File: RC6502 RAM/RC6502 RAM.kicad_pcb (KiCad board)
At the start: 2 copper layers, 99.1 x 48.3 mm, 9 parts, among them J1 Page PullUp, J2 Bus enable, J3 CONN_01X39, U1 HM62256BLP-7, U2 74HCT00

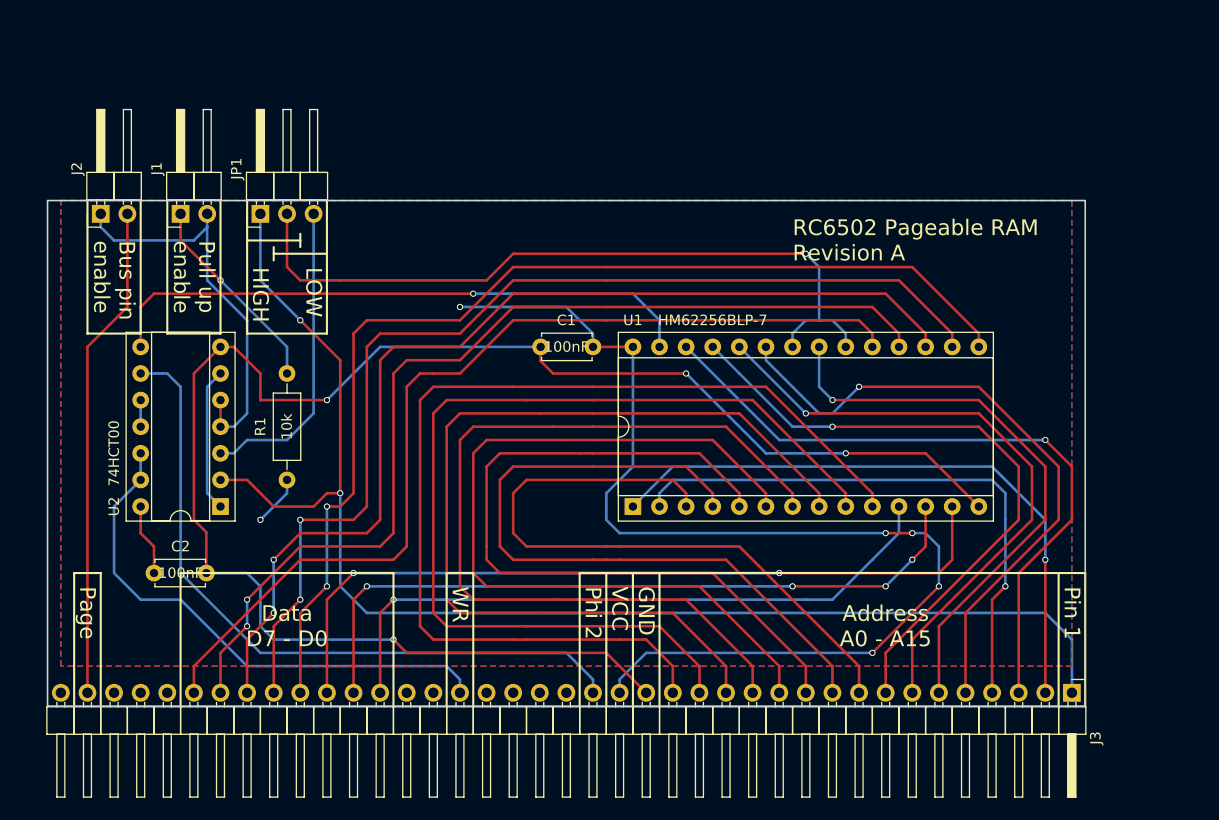
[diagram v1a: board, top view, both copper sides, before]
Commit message: RAM revision B
Fixed silkscreen notes by swapping high/low text, moved around tracks to make it a little more compact.
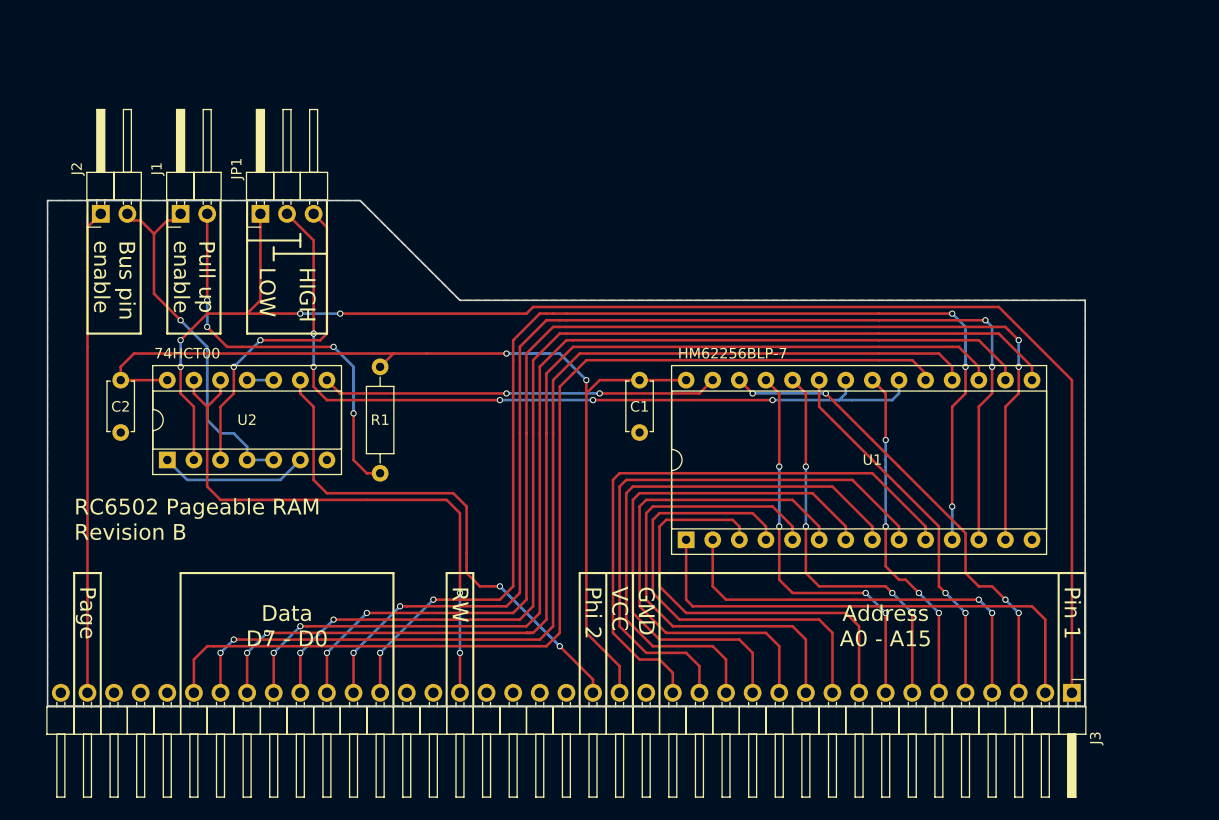
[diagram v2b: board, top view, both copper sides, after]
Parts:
- moved C2 18.7 mm to (95.9, 118.7), turned to 270 degrees
- moved R1 14.0 mm to (120.7, 117.5), turned to 270 degrees
- moved U2 6.75 mm to (100.3, 126.4), turned to 90 degrees
- moved U1 5.99 mm to (149.9, 134.0)
- moved C1 5.46 mm to (145.4, 118.7), turned to 270 degrees
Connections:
- net WR renamed RW
- J1 pad 1: Net-(J1-Pad1) -> PAGE
- J1 pad 2: PAGE -> Net-(J1-Pad2)
- J2 pad 1: PAGE -> Net-(J2-Pad1)
- J2 pad 2: Net-(J2-Pad2) -> PAGE
- J3 pad 38: Net-(J2-Pad2) -> Net-(J2-Pad1)
- R1 pad 2: Net-(J1-Pad1) -> Net-(J1-Pad2)
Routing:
- net GND: track 157.3 -> 0.00 mm, vias 4 -> 0
- net Net-(J2-Pad2): track 47.3 -> 0.00 mm
- net Net-(J2-Pad1): track 0.00 -> 46.2 mm
- net D0: track 62.8 -> 108.2 mm, vias 1 -> 5
- net D1: track 69.4 -> 112.8 mm
- net A0: track 99.0 -> 57.3 mm
- net D2: track 75.2 -> 116.6 mm, vias 2 -> 4
- net A1: track 93.9 -> 55.1 mm
- net Net-(J1-Pad2): track 0.00 -> 38.3 mm, vias 0 -> 4
- net A2: track 88.9 -> 52.9 mm
- net A3: track 83.8 -> 50.8 mm
- net A4: track 78.7 -> 48.6 mm
- net A5: track 73.6 -> 46.4 mm
- net VCC: track 120.2 -> 94.8 mm, vias 6 -> 2
- net A11: track 60.8 -> 35.6 mm, vias 1 -> 2
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- removed copper zone on F.Cu, net VCC
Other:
- outline, holes or cut-outs redrawn
- board text added: "RC6502 Pageable RAM Revision B"
- board text added: "RW"
- board text removed: "RC6502 Pageable RAM Revision A"
- board text removed: "WR"

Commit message: Enhanced RAM/ROM board, routing done
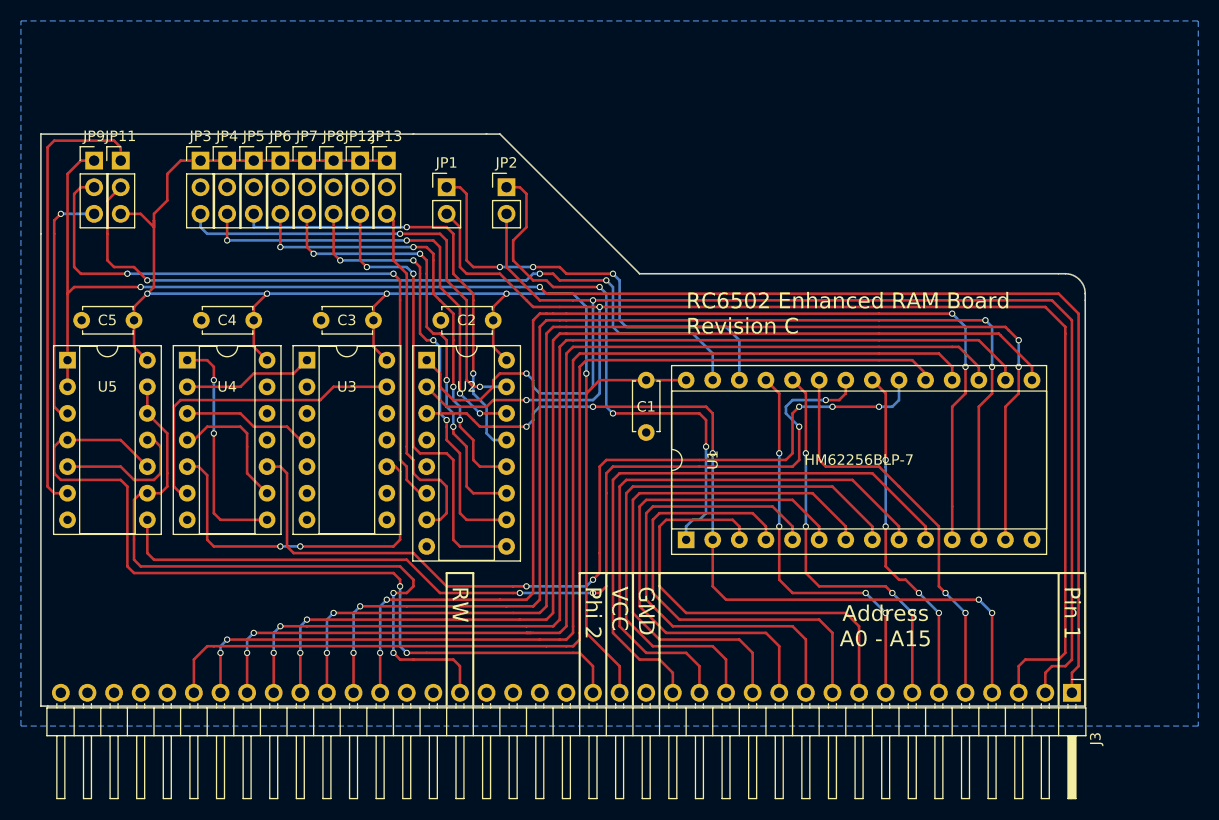
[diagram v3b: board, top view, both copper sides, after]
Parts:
- removed J1: Page PullUp, Pin_Headers:Pin_Header_Angled_1x02_Pitch2.54mm
- removed J2: Bus enable, Pin_Headers:Pin_Header_Angled_1x02_Pitch2.54mm
- removed R1: 10k, Resistors_THT:R_Axial_DIN0207_L6.3mm_D2.5mm_P10.16mm_Horizontal
- added C1: 100nF, Capacitors_THT:C_Disc_D4.7mm_W2.5mm_P5.00mm, F.Cu at (146.1, 118.7)
- added C4: 100nF, Capacitors_THT:C_Disc_D4.7mm_W2.5mm_P5.00mm, F.Cu at (108.6, 113.0)
- added C5: 100nF, Capacitors_THT:C_Disc_D4.7mm_W2.5mm_P5.00mm, F.Cu at (97.2, 113.0)
- added JP11: MEM_WE, Pin_Headers:Pin_Header_Straight_1x03_Pitch2.54mm, F.Cu at (95.9, 97.8)
- added JP12: CS6_EN, Pin_Headers:Pin_Header_Straight_1x03_Pitch2.54mm, F.Cu at (118.7, 97.8)
- added JP13: CS7_EN, Pin_Headers:Pin_Header_Straight_1x03_Pitch2.54mm, F.Cu at (121.3, 97.8)
- added JP2: A14_EN, Pin_Headers:Pin_Header_Straight_1x02_Pitch2.54mm, F.Cu at (132.7, 100.3)
- added JP3: CS0_EN, Pin_Headers:Pin_Header_Straight_1x03_Pitch2.54mm, F.Cu at (103.5, 97.8)
- added JP4: CS1_EN, Pin_Headers:Pin_Header_Straight_1x03_Pitch2.54mm, F.Cu at (106.0, 97.8)
- added JP5: CS2_EN, Pin_Headers:Pin_Header_Straight_1x03_Pitch2.54mm, F.Cu at (108.6, 97.8)
- added JP6: CS3_EN, Pin_Headers:Pin_Header_Straight_1x03_Pitch2.54mm, F.Cu at (111.1, 97.8)
- added JP7: CS4_EN, Pin_Headers:Pin_Header_Straight_1x03_Pitch2.54mm, F.Cu at (113.7, 97.8)
- added JP8: CS5_EN, Pin_Headers:Pin_Header_Straight_1x03_Pitch2.54mm, F.Cu at (116.2, 97.8)
- added JP9: HI/LO, Pin_Headers:Pin_Header_Straight_1x03_Pitch2.54mm, F.Cu at (93.3, 97.8)
- added U3: 74LS02, Housings_DIP:DIP-14_W7.62mm_Socket, F.Cu at (113.7, 116.8)
- added U4: 74LS02, Housings_DIP:DIP-14_W7.62mm_Socket, F.Cu at (102.2, 116.8)
- added U5: 74LS00, Housings_DIP:DIP-14_W7.62mm_Socket, F.Cu at (90.8, 116.8)
- J3: value CONN_01X39 -> RC6502_Backplane
- JP1: value HIGH | LOW -> A13_EN; footprint Pin_Headers:Pin_Header_Angled_1x03_Pitch2.54mm -> Pin_Headers:Pin_Header_Straight_1x02_Pitch2.54mm
- U2: value 74HCT00 -> 74LS138; footprint Housings_DIP:DIP-14_W7.62mm_Socket -> Housings_DIP:DIP-16_W7.62mm_Socket
- moved U2 26.5 mm to (125.1, 116.8), turned to 0 degrees
- moved C3 24.8 mm to (120.0, 113.0), turned to 180 degrees
- moved JP1 18.0 mm to (127.0, 100.3), turned to 0 degrees
- moved C2 15.1 mm to (131.4, 113.0), turned to 180 degrees
- renumbered C1 to C2, C2 to C3
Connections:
- J3 pad 24: RW -> R/~W
- J3 pad 38: Net-(J2-Pad1) -> (no net)
- JP1 pad 1: A15 -> Net-(JP1-Pad1)
- JP1 pad 2: CS -> A13
- U1 pad 1: A14 -> Net-(JP2-Pad1)
- U1 pad 20: CS -> ~CS
- U1 pad 22: CS -> ~OE
- U1 pad 26: A13 -> Net-(JP1-Pad1)
- U1 pad 27: WE -> ~WE
- U2 pad 1: Net-(U2-Pad1) -> A14
- U2 pad 10: Net-(U2-Pad10) -> ~CS5
- U2 pad 11: Net-(U2-Pad10) -> ~CS4
- U2 pad 12: RW -> ~CS3
- U2 pad 13: RW -> ~CS2
- U2 pad 14: VCC -> ~CS1
- U2 pad 2: A15 -> A13
- U2 pad 3: CS_HI -> A12
- U2 pad 4: PAGE -> GND
- U2 pad 5: PAGE -> GND
- U2 pad 6: Net-(U2-Pad1) -> E3
- U2 pad 7: GND -> ~CS7
- U2 pad 8: WE -> GND
- U2 pad 9: PHI2 -> ~CS6
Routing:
- net ~OE: track 0.00 -> 91.7 mm, vias 0 -> 4
- net ~CS: track 0.00 -> 86.6 mm, vias 0 -> 5
- net A13: track 45.7 -> 130.5 mm, vias 4 -> 2
- net A14: track 47.8 -> 127.8 mm, vias 0 -> 2
- net CS: track 77.7 -> 0.00 mm, vias 5 -> 0
- net ~WE: track 0.00 -> 74.3 mm, vias 0 -> 3
- net R/~W: track 0.00 -> 65.1 mm, vias 0 -> 2
- net VCC: track 94.8 -> 158.3 mm, vias 2 -> 5
- net E3: track 0.00 -> 62.5 mm, vias 0 -> 2
- net RW: track 56.1 -> 0.00 mm, vias 2 -> 0
- net Net-(JP2-Pad1): track 0.00 -> 52.7 mm, vias 0 -> 3
- net Net-(J2-Pad1): track 46.2 -> 0.00 mm
- net ~CS6: track 0.00 -> 43.9 mm, vias 0 -> 2
- net Net-(JP1-Pad1): track 0.00 -> 43.8 mm, vias 0 -> 3
- net ~CS0: track 0.00 -> 43.5 mm, vias 0 -> 2
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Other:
- board size 99.1 x 48.3 mm -> 99.7 x 54.6 mm
- board text added: "RC6502 Enhanced RAM Board Revision C"
- board text removed: "Bus pin enable"
- board text removed: "Data D7 - D0"
- board text removed: "HIGH"
- board text removed: "LOW"
- board text removed: "Page"
- board text removed: "Pull up enable"
- board text removed: "RC6502 Pageable RAM Revision B"

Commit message: Flipped decoder inputs, added details to silkscreen.
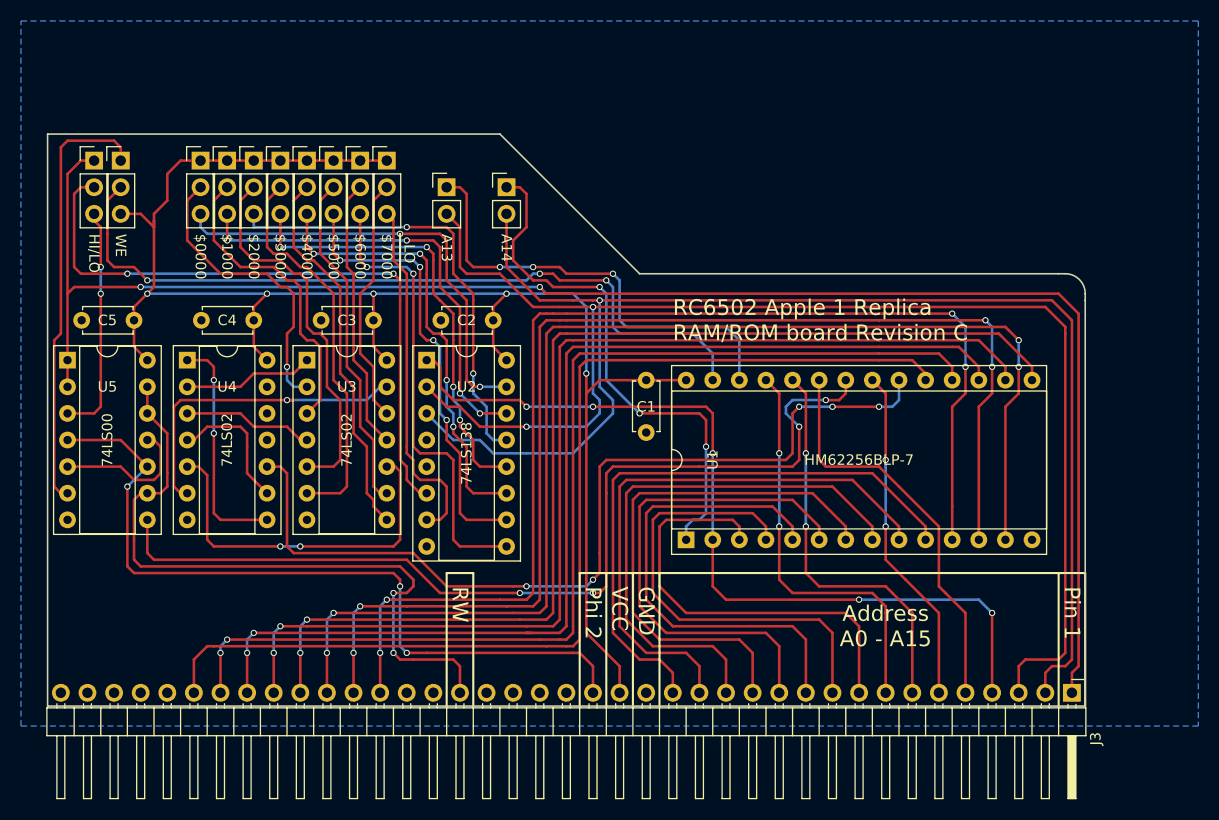
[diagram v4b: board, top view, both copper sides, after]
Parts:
- JP9: value HI/LO -> LO/HI
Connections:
- U2 pad 1: A14 -> A12
- U2 pad 3: A12 -> A14
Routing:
- net Net-(JP6-Pad2): track 0.00 -> 37.4 mm
- net Net-(JP7-Pad2): track 0.00 -> 36.3 mm
- net Net-(JP5-Pad2): track 0.00 -> 36.2 mm
- net Net-(JP8-Pad2): track 0.00 -> 32.7 mm
- net Net-(JP4-Pad2): track 0.00 -> 29.5 mm
- net Net-(JP3-Pad2): track 0.00 -> 28.6 mm, vias 0 -> 1
- net Net-(JP12-Pad2): track 0.00 -> 26.2 mm
- net Net-(JP13-Pad2): track 0.00 -> 23.7 mm
- net PHI2: track 82.5 -> 74.3 mm, vias 2 -> 3
- net A14: track 127.8 -> 130.8 mm, vias 2 -> 1
- net A13: track 130.5 -> 133.4 mm
- net Net-(JP11-Pad1): track 43.3 -> 41.7 mm
- net Net-(JP2-Pad1): track 52.7 -> 51.2 mm
- net Net-(JP9-Pad3): track 23.4 -> 22.1 mm, vias 1 -> 2
- net A12: track 81.1 -> 82.4 mm
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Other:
- board size 99.7 x 54.6 mm -> 99.1 x 54.6 mm
- board text added: "$0000"
- board text added: "$1000"
- board text added: "$2000"
- board text added: "$3000"
- board text added: "$4000"
- board text added: "$5000"
- board text added: "$6000"
- board text added: "$7000"
- board text added: "$8000"
- board text added: "$9000"
- board text added: "$A000"
- board text added: "$B000"
- board text added: "$C000"
- board text added: "$D000"
- board text added: "$E000"
- board text added: "$F000"
- board text added: "1-2 1-2 NC"
- board text added: "1-2 2-3 2-3"
- board text added: "1-2 HI 2-3 LO"
- board text added: "1-2 WE 2-3 MP"
- board text added: "A13"
- board text added: "A14"
- board text added: "HI"
- board text added: "HI/LO"
- board text added: "LO"
- board text added: "RAM 62256 ROM 28C256 ROM 28C64"
- board text added: "RC6502 Apple 1 Replica RAM/ROM board Revision C"
- board text added: "WE"
- board text added: "https://hvetebolle.blogspot.com"
- board text removed: "RC6502 Enhanced RAM Board Revision C"

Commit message: Fixed RAM board block select logic
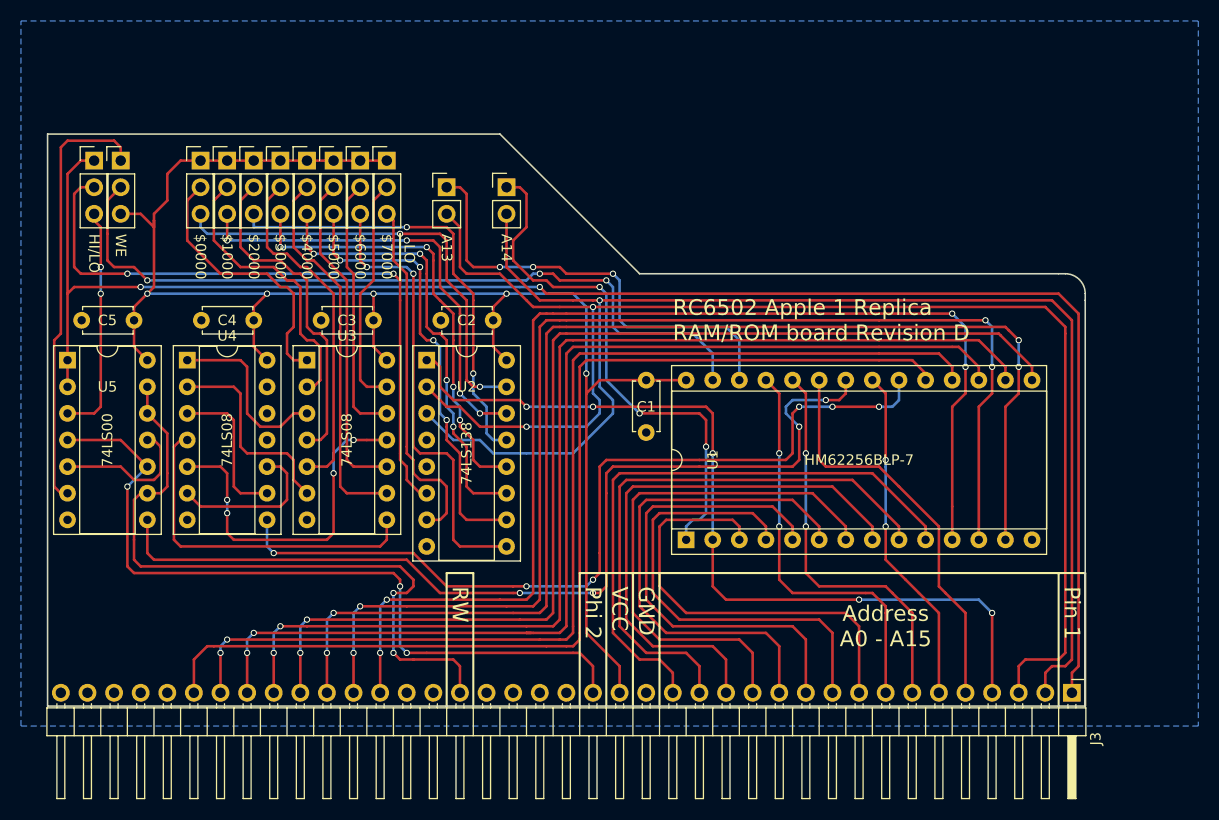
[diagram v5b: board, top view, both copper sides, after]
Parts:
- U3, U4: value 74LS02 -> 74LS08
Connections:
- U3 pad 1: Net-(U3-Pad1) -> Net-(JP3-Pad2)
- U3 pad 10: Net-(U3-Pad10) -> Net-(JP8-Pad2)
- U3 pad 11: Net-(JP12-Pad2) -> Net-(U3-Pad11)
- U3 pad 12: Net-(JP13-Pad2) -> Net-(JP12-Pad2)
- U3 pad 13: Net-(U3-Pad13) -> Net-(JP13-Pad2)
- U3 pad 2: Net-(JP3-Pad2) -> Net-(JP4-Pad2)
- U3 pad 3: Net-(JP4-Pad2) -> Net-(U3-Pad3)
- U3 pad 4: Net-(U3-Pad4) -> Net-(JP5-Pad2)
- U3 pad 5: Net-(JP5-Pad2) -> Net-(JP6-Pad2)
- U3 pad 6: Net-(JP6-Pad2) -> Net-(U3-Pad6)
- U3 pad 8: Net-(JP7-Pad2) -> Net-(U3-Pad8)
- U3 pad 9: Net-(JP8-Pad2) -> Net-(JP7-Pad2)
- U4 pad 1: Net-(U4-Pad1) -> Net-(U3-Pad3)
- U4 pad 10: ~CS -> Net-(U4-Pad10)
- U4 pad 11: GND -> (no net)
- U4 pad 13: (no net) -> GND
- U4 pad 2: Net-(U3-Pad1) -> Net-(U3-Pad6)
- U4 pad 3: Net-(U3-Pad4) -> Net-(U4-Pad3)
- U4 pad 4: Net-(U4-Pad4) -> Net-(U3-Pad8)
- U4 pad 5: Net-(U3-Pad10) -> Net-(U3-Pad11)
- U4 pad 6: Net-(U3-Pad13) -> Net-(U4-Pad10)
- U4 pad 8: Net-(U4-Pad1) -> ~CS
- U4 pad 9: Net-(U4-Pad4) -> Net-(U4-Pad3)
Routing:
- net Net-(U3-Pad10): track 35.3 -> 0.00 mm, vias 2 -> 0
- net Net-(U3-Pad11): track 0.00 -> 33.7 mm, vias 0 -> 4
- net Net-(U3-Pad8): track 0.00 -> 33.2 mm
- net Net-(U3-Pad13): track 31.5 -> 0.00 mm, vias 1 -> 0
- net Net-(U4-Pad1): track 22.1 -> 0.00 mm, vias 2 -> 0
- net Net-(U3-Pad6): track 0.00 -> 19.7 mm
- net Net-(U3-Pad3): track 0.00 -> 17.2 mm
- net Net-(U4-Pad10): track 0.00 -> 15.0 mm
- net Net-(U4-Pad3): track 0.00 -> 14.5 mm
- net Net-(U4-Pad4): track 13.0 -> 0.00 mm
- net Net-(U3-Pad4): track 12.5 -> 0.00 mm
- net Net-(U3-Pad1): track 12.5 -> 0.00 mm
- net ~CS: track 86.6 -> 81.9 mm, vias 5 -> 6
- net Net-(JP6-Pad2): track 37.4 -> 33.1 mm
- net Net-(JP5-Pad2): track 36.2 -> 31.8 mm
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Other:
- board text added: "RC6502 Apple 1 Replica RAM/ROM board Revision D"
- board text removed: "RC6502 Apple 1 Replica RAM/ROM board Revision C"
